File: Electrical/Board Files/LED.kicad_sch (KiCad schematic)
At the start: 22 parts, among them M1 Motor_DC, Q3 BSS138, Q4 BSS138, Q5 BSS138, Q6 BSS138, Q7 BSS138, Q8 BSS138

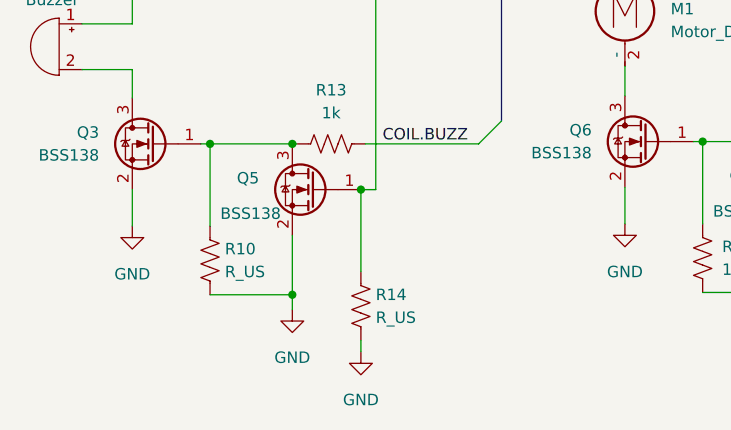
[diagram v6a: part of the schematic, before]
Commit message: Fixing USB pins and added SPI_CS
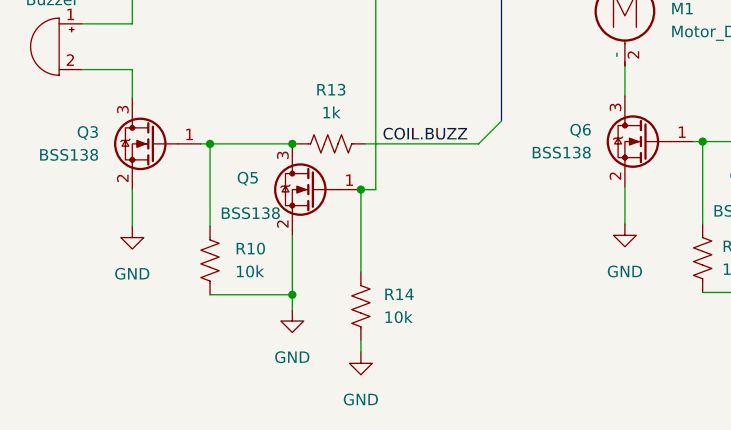
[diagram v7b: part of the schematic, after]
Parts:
- R10, R14: value R_US -> 10k
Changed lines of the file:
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@@
   (symbol (lib_id "Device:R_US") (at 72.39 164.338 0) (unit 1)
     (in_bom yes) (on_board yes) (fields_autoplaced)
-    (property "Reference" "R14" (id 0) (at 74.041 163.0679 0)
+    (property "Reference" "R14" (id 0) (at 74.93 163.0679 0)
       (effects (font (size 1.27 1.27)) (justify left))
     )
-    (property "Value" "R_US" (id 1) (at 74.041 165.6079 0)
+    (property "Value" "10k" (id 1) (at 74.93 165.6079 0)
       (effects (font (size 1.27 1.27)) (justify left))
     )
@@
   (symbol (lib_id "Device:R_US") (at 55.626 159.258 0) (unit 1)
     (in_bom yes) (on_board yes) (fields_autoplaced)
-    (property "Reference" "R10" (id 0) (at 57.277 157.9879 0)
+    (property "Reference" "R10" (id 0) (at 58.42 157.9879 0)
       (effects (font (size 1.27 1.27)) (justify left))
     )
-    (property "Value" "R_US" (id 1) (at 57.277 160.5279 0)
+    (property "Value" "10k" (id 1) (at 58.42 160.5279 0)
       (effects (font (size 1.27 1.27)) (justify left))
     )

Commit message: Adding some device footprints and MPN
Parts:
- D17, D18: value XZM2ACRM2DGFBB110W -> RGB LED; MANUFACTURER (none) -> XZM2ACRM2DGFBB110W
- R10, R11, R12, R13, R14, R15, R16, R17, R18, R19, R20, R9: footprint (none) -> Resistor_SMD:R_0603_1608Metric
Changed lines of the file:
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@@
       (effects (font (size 1.27 1.27)) (justify left))
     )
-    (property "Footprint" "" (id 2) (at 111.379 159.258 90)
+    (property "Footprint" "Resistor_SMD:R_0603_1608Metric" (id 2) (at 111.379 159.258 90)
       (effects (font (size 1.27 1.27)) hide)
     )
@@
       (effects (font (size 1.27 1.27)) (justify left))
     )
-    (property "Footprint" "" (id 2) (at 73.406 164.592 90)
+    (property "Footprint" "Resistor_SMD:R_0603_1608Metric" (id 2) (at 73.406 164.592 90)
       (effects (font (size 1.27 1.27)) hide)
     )
@@
       (effects (font (size 1.27 1.27)) (justify left))
     )
-    (property "Footprint" "" (id 2) (at 121.92 77.597 90)
+    (property "Footprint" "Resistor_SMD:R_0603_1608Metric" (id 2) (at 121.92 77.597 90)
       (effects (font (size 1.27 1.27)) hide)
     )
@@
       (effects (font (size 1.27 1.27)) (justify left))
     )
-    (property "Footprint" "" (id 2) (at 105.918 53.975 90)
+    (property "Footprint" "Resistor_SMD:R_0603_1608Metric" (id 2) (at 105.918 53.975 90)
       (effects (font (size 1.27 1.27)) hide)
     )
@@
       (effects (font (size 1.27 1.27)) (justify left))
     )
-    (property "Footprint" "" (id 2) (at 56.642 159.512 90)
+    (property "Footprint" "Resistor_SMD:R_0603_1608Metric" (id 2) (at 56.642 159.512 90)
       (effects (font (size 1.27 1.27)) hide)
     )
@@
       (effects (font (size 1.27 1.27)) (justify left))
     )
-    (property "Footprint" "" (id 2) (at 51.689 57.785 90)
+    (property "Footprint" "Resistor_SMD:R_0603_1608Metric" (id 2) (at 51.689 57.785 90)
       (effects (font (size 1.27 1.27)) hide)
     )
@@
       (effects (font (size 1.27 1.27)) (justify left))
     )
-    (property "Footprint" "" (id 2) (at 68.453 81.534 90)
+    (property "Footprint" "Resistor_SMD:R_0603_1608Metric" (id 2) (at 68.453 81.534 90)
       (effects (font (size 1.27 1.27)) hide)
     )
@@
     (property "Reference" "R17" (id 0) (at 116.459 58.801 90))
     (property "Value" "100" (id 1) (at 116.459 61.341 90))
-    (property "Footprint" "" (id 2) (at 116.713 63.373 90)
+    (property "Footprint" "Resistor_SMD:R_0603_1608Metric" (id 2) (at 116.713 63.373 90)
       (effects (font (size 1.27 1.27)) hide)
     )
@@
     (property "Reference" "R13" (id 0) (at 69.088 140.335 90))
     (property "Value" "1k" (id 1) (at 69.088 142.875 90))
-    (property "Footprint" "" (id 2) (at 69.342 145.288 90)
+    (property "Footprint" "Resistor_SMD:R_0603_1608Metric" (id 2) (at 69.342 145.288 90)
       (effects (font (size 1.27 1.27)) hide)
     )
@@
     (property "Reference" "R11" (id 0) (at 62.611 62.611 90))
     (property "Value" "100" (id 1) (at 62.611 65.151 90))
-    (property "Footprint" "" (id 2) (at 62.865 67.31 90)
+    (property "Footprint" "Resistor_SMD:R_0603_1608Metric" (id 2) (at 62.865 67.31 90)
       (effects (font (size 1.27 1.27)) hide)
     )
@@
       (effects (font (size 1.27 1.27)) (justify right))
     )
-    (property "Value" "XZM2ACRM2DGFBB110W" (id 1) (at 113.665 44.4499 90)
+    (property "Value" "RGB LED" (id 1) (at 113.665 44.4499 90)
       (effects (font (size 1.27 1.27)) (justify right))
     )
@@
     )
     (property "Datasheet" "https://www.sunledusa.com/products/spec/XZM2ACRM2DGFBB110W.pdf" (id 3) (at 106.172 43.18 0)
+      (effects (font (size 1.27 1.27)) hide)
+    )
+    (property "MANUFACTURER" "XZM2ACRM2DGFBB110W" (id 4) (at 104.902 43.18 0)
       (effects (font (size 1.27 1.27)) hide)
     )
@@
       (effects (font (size 1.27 1.27)) (justify right))
     )
-    (property "Value" "XZM2ACRM2DGFBB110W" (id 1) (at 59.436 44.4499 90)
+    (property "Value" "RGB LED" (id 1) (at 59.436 44.4499 90)
       (effects (font (size 1.27 1.27)) (justify right))
     )
@@
     )
     (property "Datasheet" "https://www.sunledusa.com/products/spec/XZM2ACRM2DGFBB110W.pdf" (id 3) (at 51.943 43.18 0)
+      (effects (font (size 1.27 1.27)) hide)
+    )
+    (property "MANUFACTURER" "XZM2ACRM2DGFBB110W" (id 4) (at 50.673 43.18 0)
       (effects (font (size 1.27 1.27)) hide)
     )
@@
     (property "Reference" "R19" (id 0) (at 125.095 140.081 90))
     (property "Value" "1k" (id 1) (at 125.095 142.621 90))
-    (property "Footprint" "" (id 2) (at 125.349 145.034 90)
+    (property "Footprint" "Resistor_SMD:R_0603_1608Metric" (id 2) (at 125.349 145.034 90)
       (effects (font (size 1.27 1.27)) hide)
     )
@@
       (effects (font (size 1.27 1.27)) (justify left))
     )
-    (property "Footprint" "" (id 2) (at 128.143 164.338 90)
-      (effects (font (size 1.27 1.27)) hide)
-    )
+    (property "Footprint" "Resistor_SMD:R_0603_1608Metric" (id 2) (at 128.143 164.338 90)
+      (effects (font (size 1.27 1.27)) hide)
+    )
